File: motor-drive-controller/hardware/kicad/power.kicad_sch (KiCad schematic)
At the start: 3 parts

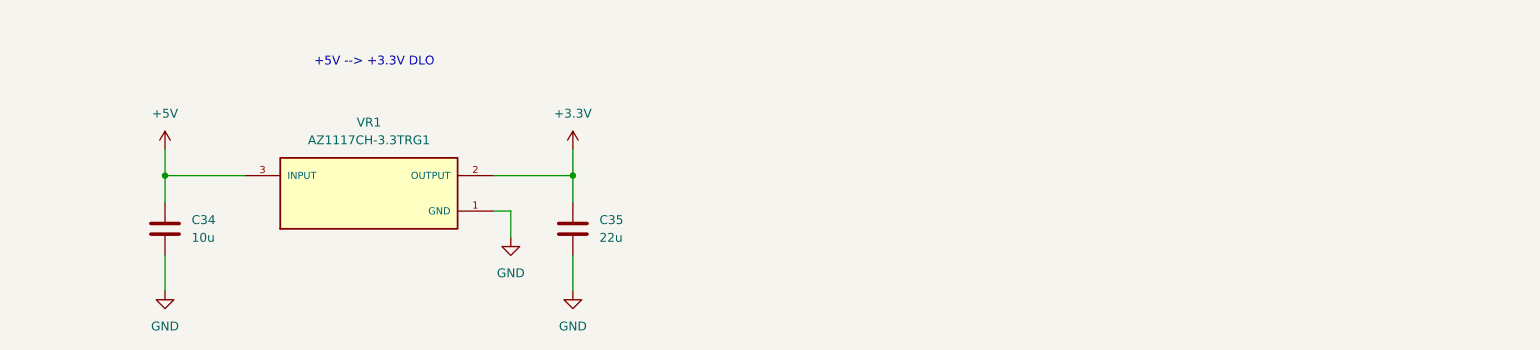
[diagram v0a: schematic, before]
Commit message: feat(hw10): add DC/DC-converter schema from 12V to 5V
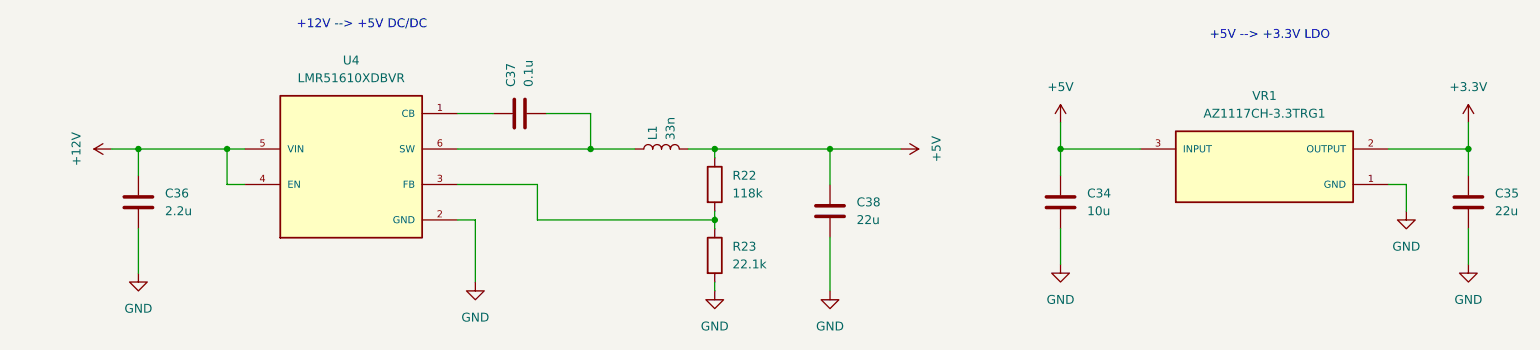
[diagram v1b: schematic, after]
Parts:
- added C36: 2.2u, Capacitor_SMD:C_0603_1608Metric, symbol Device:C
- added C37: 0.1u, Capacitor_SMD:C_0603_1608Metric, symbol Device:C
- added C38: 22u, Capacitor_SMD:C_0603_1608Metric, symbol Device:C
- added L1: 33n, symbol Device:L
- added R22: 118k, Resistor_SMD:R_0603_1608Metric, symbol Device:R
- added R23: 22.1k, Resistor_SMD:R_0603_1608Metric, symbol Device:R
- added U4: LMR51610XDBVR, LMR51610XDBVR:SOT95P280X145-6N, symbol LMR51610XDBVR:LMR51610XDBVR
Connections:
- net +5V: now also C38.1, L1.2, R22.1
- net GND: now also C36.2, C38.2, R23.2, U4.2 (GND)
- new net: C37.2, L1.1, U4.6 (SW)
- new net: C37.1, U4.1 (CB)
- new net: R22.2, R23.1, U4.3 (FB)
- new net +12V: C36.1, U4.4 (EN), U4.5 (VIN)
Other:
- note added: "+12V --> +5V DC/DC"
- note added: "+5V --> +3.3V LDO"
- note removed: "+5V --> +3.3V DLO"
- moved on the sheet: C34, C35, VR1

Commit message: fix(hw10): correct capacitor value from 33n to 33u in power schematic
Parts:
- L1: value 33n -> 33u
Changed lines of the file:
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@@
 			)
 		)
-		(property "Value" "33n"
+		(property "Value" "33u"
 			(at 114.2999 125.73 0)
 			(show_name no)

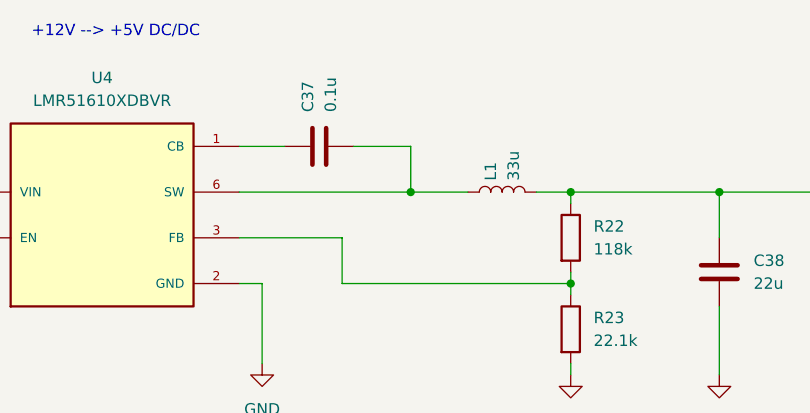
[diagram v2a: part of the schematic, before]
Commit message: fix(hw10): replace  inductor for XAL6060-333MEC
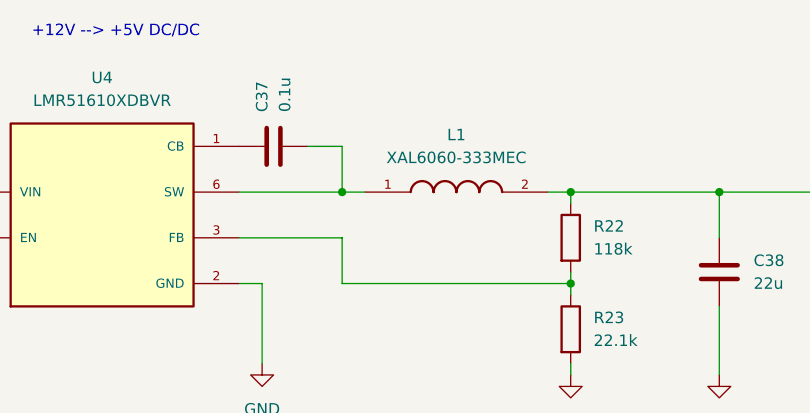
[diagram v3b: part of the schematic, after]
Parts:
- removed L1: 33u, symbol Device:L
- added L1: XAL6060-333MEC, XAL6060-333MEC:XAL6060333MEC, symbol XAL6060-333MEC:XAL6060-333MEC
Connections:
- net +5V: now also L1.2
- net at C37.2, U4.6 (SW): now also L1.1
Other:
- moved on the sheet: C37

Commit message: fix(hw10): update capacitor footprints and add voltage properties in power schematic
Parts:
- C34: footprint Capacitor_SMD:C_0603_1608Metric -> Capacitor_SMD:C_1206_3216Metric; Voltage (none) -> 16V
- C35: footprint Capacitor_SMD:C_0603_1608Metric -> Capacitor_SMD:C_0805_2012Metric; Voltage (none) -> 10V
- C36: footprint Capacitor_SMD:C_0603_1608Metric -> Capacitor_SMD:C_1206_3216Metric; Voltage (none) -> 50V
- C38: footprint Capacitor_SMD:C_0603_1608Metric -> Capacitor_SMD:C_1210_3225Metric; Voltage (none) -> 25V
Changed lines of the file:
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@@
 			)
 		)
-		(property "Footprint" "Capacitor_SMD:C_0603_1608Metric"
+		(property "Footprint" "Capacitor_SMD:C_1206_3216Metric"
 			(at 39.0652 138.43 0)
 			(hide yes)
@@
 			)
 		)
+		(property "Voltage" "50V"
+			(at 38.1 134.62 0)
+			(hide yes)
+			(show_name no)
+			(do_not_autoplace no)
+			(effects
+				(font
+					(size 1.27 1.27)
+				)
+			)
+		)
 		(pin "1"
 		)
@@
 			)
 		)
-		(property "Footprint" "Capacitor_SMD:C_0603_1608Metric"
+		(property "Footprint" "Capacitor_SMD:C_1210_3225Metric"
 			(at 138.1252 139.7 0)
 			(hide yes)
@@
 			)
 		)
+		(property "Voltage" "25V"
+			(at 137.16 135.89 0)
+			(hide yes)
+			(show_name no)
+			(do_not_autoplace no)
+			(effects
+				(font
+					(size 1.27 1.27)
+				)
+			)
+		)
 		(pin "1"
 		)
@@
 			)
 		)
-		(property "Footprint" "Capacitor_SMD:C_0603_1608Metric"
+		(property "Footprint" "Capacitor_SMD:C_0805_2012Metric"
 			(at 229.5652 138.43 0)
 			(hide yes)
@@
 			)
 		)
+		(property "Voltage" "10V"
+			(at 228.6 134.62 0)
+			(hide yes)
+			(show_name no)
+			(do_not_autoplace no)
+			(effects
+				(font
+					(size 1.27 1.27)
+				)
+			)
+		)
 		(pin "1"
 		)
@@
 			)
 		)
-		(property "Footprint" "Capacitor_SMD:C_0603_1608Metric"
+		(property "Footprint" "Capacitor_SMD:C_1206_3216Metric"
 			(at 171.1452 138.43 0)
 			(hide yes)
@@
 			(at 170.18 134.62 0)
 			(hide yes)
+			(show_name no)
+			(do_not_autoplace no)
+			(effects
+				(font
+					(size 1.27 1.27)
+				)
+			)
+		)
+		(property "Voltage" "16V"
+			(at 170.18 134.62 0)
+			(hide yes)

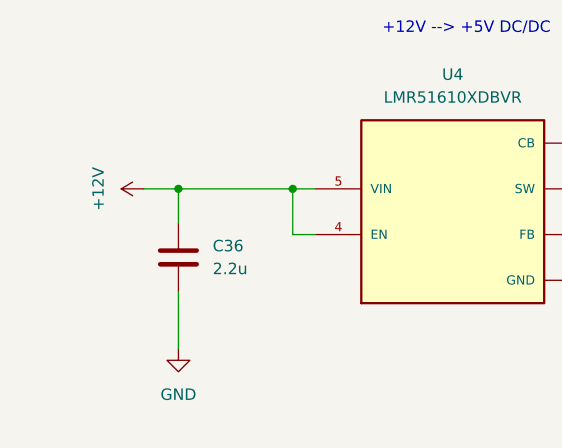
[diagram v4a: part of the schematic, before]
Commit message: fix(hw10): add 100nF capacitor for high-frequency filtering in power schematic
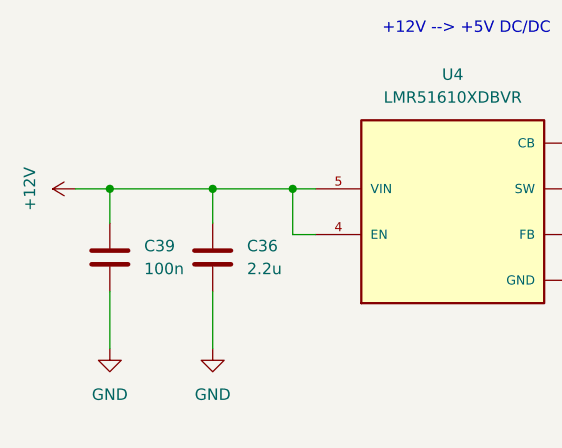
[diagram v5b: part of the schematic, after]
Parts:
- added C39: 100n, Capacitor_SMD:C_0603_1608Metric, symbol Device:C
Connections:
- net +12V: now also C39.1
- net GND: now also C39.2
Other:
- moved on the sheet: C36
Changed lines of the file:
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@@
+	)
+	(junction
+		(at 41.91 127)
+		(diameter 0)
+		(color 0 0 0 0)
 	)
 	(junction
@@
 	)
 	(junction
-		(at 38.1 127)
+		(at 30.48 127)
 		(diameter 0)
 		(color 0 0 0 0)
@@
 	(wire
 		(pts
+			(xy 30.48 138.43) (xy 30.48 144.78)
+		)
+		(stroke
+			(width 0)
+			(type default)
+		)
+	)
+	(wire
+		(pts
 			(xy 137.16 127) (xy 137.16 132.08)
 		)
@@
 	(wire
 		(pts
-			(xy 34.29 127) (xy 38.1 127)
+			(xy 26.67 127) (xy 30.48 127)
 		)
 		(stroke
@@
 	(wire
 		(pts
-			(xy 38.1 138.43) (xy 38.1 144.78)
+			(xy 41.91 138.43) (xy 41.91 144.78)
 		)
 		(stroke
@@
 	(wire
 		(pts
+			(xy 30.48 127) (xy 41.91 127)
+		)
+		(stroke
+			(width 0)
+			(type default)
+		)
+	)
+	(wire
+		(pts
 			(xy 118.11 127) (xy 120.65 127)
 		)
@@
 	(wire
 		(pts
-			(xy 38.1 127) (xy 38.1 130.81)
+			(xy 41.91 127) (xy 41.91 130.81)
 		)
 		(stroke
@@
 	(wire
 		(pts
+			(xy 30.48 127) (xy 30.48 130.81)
+		)
+		(stroke
+			(width 0)
+			(type default)
+		)
+	)
+	(wire
+		(pts
 			(xy 120.65 146.05) (xy 120.65 147.32)
 		)
@@
 	(wire
 		(pts
-			(xy 38.1 127) (xy 50.8 127)
-		)
-		(stroke
-			(width 0)
-			(type default)
-		)
-	)
-	(wire
-		(pts
 			(xy 91.44 121.92) (xy 95.25 121.92)
 		)
@@
 		(pts
 			(xy 120.65 135.89) (xy 120.65 137.16)
+		)
+		(stroke
+			(width 0)
+			(type default)
+		)
+	)
+	(wire
+		(pts
+			(xy 41.91 127) (xy 50.8 127)
 		)
 		(stroke
@@
 	(symbol
 		(lib_id "Device:C")
-		(at 38.1 134.62 0)
+		(at 41.91 134.62 0)
 		(unit 1)
 		(body_style 1)
@@
 		(fields_autoplaced yes)
 		(property "Reference" "C36"
-			(at 41.91 133.3499 0)
+			(at 45.72 133.3499 0)
 			(show_name no)
 			(do_not_autoplace no)
@@
 		)
 		(property "Value" "2.2u"
-			(at 41.91 135.8899 0)
+			(at 45.72 135.8899 0)
 			(show_name no)
 			(do_not_autoplace no)
@@
 		)
 		(property "Footprint" "Capacitor_SMD:C_1206_3216Metric"
-			(at 39.0652 138.43 0)
+			(at 42.8752 138.43 0)
 			(hide yes)
 			(show_name no)
@@
 		)
 		(property "Datasheet" ""
-			(at 38.1 134.62 0)
+			(at 41.91 134.62 0)
 			(hide yes)
 			(show_name no)
@@
 		)
 		(property "Description" "Unpolarized capacitor"
-			(at 38.1 134.62 0)
+			(at 41.91 134.62 0)
 			(hide yes)
 			(show_name no)
@@
 		)
 		(property "Voltage" "50V"
-			(at 38.1 134.62 0)
+			(at 41.91 134.62 0)
 			(hide yes)
 			(show_name no)
@@
 	)
 	(symbol
+		(lib_id "Device:C")
+		(at 30.48 134.62 0)
+		(unit 1)
+		(body_style 1)
+		(exclude_from_sim no)
+		(in_bom yes)
+		(on_board yes)
+		(in_pos_files yes)
+		(dnp no)
+		(fields_autoplaced yes)
+		(property "Reference" "C39"
+			(at 34.29 133.3499 0)
+			(show_name no)
+			(do_not_autoplace no)
+			(effects
+				(font
+					(size 1.27 1.27)
+				)
+				(justify left)
+			)
+		)
+		(property "Value" "100n"
+			(at 34.29 135.8899 0)
+			(show_name no)
+			(do_not_autoplace no)
+			(effects
+				(font
+					(size 1.27 1.27)
+				)
+				(justify left)
+			)
+		)
+		(property "Footprint" "Capacitor_SMD:C_0603_1608Metric"
+			(at 31.4452 138.43 0)
+			(hide yes)
+			(show_name no)
+			(do_not_autoplace no)
+			(effects
+				(font
+					(size 1.27 1.27)
+				)
+			)
+		)
+		(property "Datasheet" ""
+			(at 30.48 134.62 0)
+			(hide yes)
+			(show_name no)
+			(do_not_autoplace no)
+			(effects
+				(font
+					(size 1.27 1.27)
+				)
+			)
+		)
+		(property "Description" "Unpolarized capacitor"
+			(at 30.48 134.62 0)
+			(hide yes)
+			(show_name no)
+			(do_not_autoplace no)
+			(effects
+				(font
+					(size 1.27 1.27)
+				)
+			)
+		)
+		(pin "1"
+		)
+		(pin "2"
+		)
+		(instances
+			(project "motor-drive-controller"
+				(path "/b8e0307a-d356-4cd3-91c6-dd251b6e910b/4f45cab3-b4c2-456a-894e-61f49c3959a4"
+					(reference "C39")
+					(unit 1)
+				)
+			)
+		)
+	)
+	(symbol
 		(lib_id "power:GND")
 		(at 137.16 147.32 0)
@@
 	(symbol
 		(lib_id "power:GND")
-		(at 38.1 144.78 0)
+		(at 41.91 144.78 0)
 		(unit 1)
 		(body_style 1)
@@
 		(fields_autoplaced yes)
 		(property "Reference" "#PWR063"
-			(at 38.1 151.13 0)
+			(at 41.91 151.13 0)
 			(hide yes)
 			(show_name no)
@@
 		)
 		(property "Value" "GND"
-			(at 38.1 149.86 0)
+			(at 41.91 149.86 0)
 			(show_name no)
 			(do_not_autoplace no)
@@
 		)
 		(property "Footprint" ""
-			(at 38.1 144.78 0)
+			(at 41.91 144.78 0)
 			(hide yes)
 			(show_name no)
@@
 		)
 		(property "Datasheet" ""
-			(at 38.1 144.78 0)
+			(at 41.91 144.78 0)
 			(hide yes)
 			(show_name no)
@@
 		)
 		(property "Description" "Power symbol creates a global label with name \"GND\" , ground"
-			(at 38.1 144.78 0)
+			(at 41.91 144.78 0)
 			(hide yes)
 			(show_name no)
@@
 	(symbol
 		(lib_id "power:+12V")
-		(at 34.29 127 90)
+		(at 26.67 127 90)
 		(unit 1)
 		(body_style 1)
@@
 		(fields_autoplaced yes)
 		(property "Reference" "#PWR062"
-			(at 38.1 127 0)
+			(at 30.48 127 0)
 			(hide yes)
 			(show_name no)
@@
 		)
 		(property "Value" "+12V"
-			(at 29.21 127 0)
+			(at 21.59 127 0)
 			(show_name no)
 			(do_not_autoplace no)
@@
 		)
 		(property "Footprint" ""
-			(at 34.29 127 0)
+			(at 26.67 127 0)
 			(hide yes)
 			(show_name no)
@@
 		)
 		(property "Datasheet" ""
-			(at 34.29 127 0)
+			(at 26.67 127 0)
 			(hide yes)
 			(show_name no)
@@
 		)
 		(property "Description" "Power symbol creates a global label with name \"+12V\""
-			(at 34.29 127 0)
+			(at 26.67 127 0)
 			(hide yes)
 			(show_name no)
@@
 					(unit 1)
 				)
+			)
+		)
+	)
+	(symbol
+		(lib_id "power:GND")
+		(at 30.48 144.78 0)
+		(unit 1)
+		(body_style 1)
+		(exclude_from_sim no)
+		(in_bom yes)
+		(on_board yes)
+		(in_pos_files yes)
+		(dnp no)
+		(fields_autoplaced yes)
+		(property "Reference" "#PWR068"
+			(at 30.48 151.13 0)
+			(hide yes)
+			(show_name no)
+			(do_not_autoplace no)
+			(effects
+				(font
+					(size 1.27 1.27)
+				)
+			)
+		)
+		(property "Value" "GND"
+			(at 30.48 149.86 0)
+			(show_name no)
+			(do_not_autoplace no)
+			(effects
+				(font
+					(size 1.27 1.27)
+				)
+			)
+		)
+		(property "Footprint" ""
+			(at 30.48 144.78 0)
+			(hide yes)
+			(show_name no)
+			(do_not_autoplace no)
+			(effects
+				(font
+					(size 1.27 1.27)
+				)
+			)
+		)
+		(property "Datasheet" ""
+			(at 30.48 144.78 0)
+			(hide yes)
+			(show_name no)
+			(do_not_autoplace no)
+			(effects
+				(font
+					(size 1.27 1.27)
+				)
+			)
+		)
+		(property "Description" "Power symbol creates a global label with name \"GND\" , ground"
+			(at 30.48 144.78 0)
+			(hide yes)
+			(show_name no)
+			(do_not_autoplace no)
+			(effects
+				(font
+					(size 1.27 1.27)
+				)
+			)
+		)
+		(pin "1"
+		)
+		(instances
+			(project "motor-drive-controller"
+				(path "/b8e0307a-d356-4cd3-91c6-dd251b6e910b/4f45cab3-b4c2-456a-894e-61f49c3959a4"
+					(reference "#PWR068")
+					(unit 1)
+				)

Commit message: fix(hw10): reset existing annotation
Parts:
- renumbered C39 to C34, C36 to C35, C37 to C36, C38 to C37, C34 to C38, C35 to C39
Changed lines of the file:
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@@
 		(dnp no)
 		(fields_autoplaced yes)
-		(property "Reference" "C36"
+		(property "Reference" "C35"
 			(at 45.72 133.3499 0)
 			(show_name no)
@@
 			(project "motor-drive-controller"
 				(path "/b8e0307a-d356-4cd3-91c6-dd251b6e910b/4f45cab3-b4c2-456a-894e-61f49c3959a4"
-					(reference "C36")
+					(reference "C35")
 					(unit 1)
 				)
@@
 		(dnp no)
 		(fields_autoplaced yes)
-		(property "Reference" "C38"
+		(property "Reference" "C37"
 			(at 140.97 134.6199 0)
 			(show_name no)
@@
 			(project "motor-drive-controller"
 				(path "/b8e0307a-d356-4cd3-91c6-dd251b6e910b/4f45cab3-b4c2-456a-894e-61f49c3959a4"
-					(reference "C38")
+					(reference "C37")
 					(unit 1)
 				)
@@
 		(dnp no)
 		(fields_autoplaced yes)
-		(property "Reference" "C35"
+		(property "Reference" "C39"
 			(at 232.41 133.3499 0)
 			(show_name no)
@@
 			(project "motor-drive-controller"
 				(path "/b8e0307a-d356-4cd3-91c6-dd251b6e910b/4f45cab3-b4c2-456a-894e-61f49c3959a4"
-					(reference "C35")
+					(reference "C39")
 					(unit 1)
 				)
@@
 		(dnp no)
 		(fields_autoplaced yes)
-		(property "Reference" "#PWR066"
+		(property "Reference" "#PWR061"
 			(at 120.65 153.67 0)
 			(hide yes)
@@
 			(project "motor-drive-controller"
 				(path "/b8e0307a-d356-4cd3-91c6-dd251b6e910b/4f45cab3-b4c2-456a-894e-61f49c3959a4"
-					(reference "#PWR066")
+					(reference "#PWR061")
 					(unit 1)
 				)
@@
 		(dnp no)
 		(fields_autoplaced yes)
-		(property "Reference" "#PWR060"
+		(property "Reference" "#PWR065"
 			(at 170.18 149.86 0)
 			(hide yes)
@@
 			(project "motor-drive-controller"
 				(path "/b8e0307a-d356-4cd3-91c6-dd251b6e910b/4f45cab3-b4c2-456a-894e-61f49c3959a4"
-					(reference "#PWR060")
+					(reference "#PWR065")
 					(unit 1)
 				)
@@
 		(dnp no)
 		(fields_autoplaced yes)
-		(property "Reference" "#PWR059"
+		(property "Reference" "#PWR066"
 			(at 219.71 142.24 0)
 			(hide yes)
@@
 			(project "motor-drive-controller"
 				(path "/b8e0307a-d356-4cd3-91c6-dd251b6e910b/4f45cab3-b4c2-456a-894e-61f49c3959a4"
-					(reference "#PWR059")
+					(reference "#PWR066")
 					(unit 1)
 				)
@@
 		(dnp no)
 		(fields_autoplaced yes)
-		(property "Reference" "C39"
+		(property "Reference" "C34"
 			(at 34.29 133.3499 0)
 			(show_name no)
@@
 			(project "motor-drive-controller"
 				(path "/b8e0307a-d356-4cd3-91c6-dd251b6e910b/4f45cab3-b4c2-456a-894e-61f49c3959a4"
-					(reference "C39")
+					(reference "C34")
 					(unit 1)
 				)
@@
 		(dnp no)
 		(fields_autoplaced yes)
-		(property "Reference" "#PWR067"
+		(property "Reference" "#PWR062"
 			(at 137.16 153.67 0)
 			(hide yes)
@@
 			(project "motor-drive-controller"
 				(path "/b8e0307a-d356-4cd3-91c6-dd251b6e910b/4f45cab3-b4c2-456a-894e-61f49c3959a4"
-					(reference "#PWR067")
+					(reference "#PWR062")
 					(unit 1)
 				)
@@
 		(dnp no)
 		(fields_autoplaced yes)
-		(property "Reference" "#PWR061"
+		(property "Reference" "#PWR068"
 			(at 228.6 149.86 0)
 			(hide yes)
@@
 			(project "motor-drive-controller"
 				(path "/b8e0307a-d356-4cd3-91c6-dd251b6e910b/4f45cab3-b4c2-456a-894e-61f49c3959a4"
-					(reference "#PWR061")
+					(reference "#PWR068")
 					(unit 1)
 				)
@@
 		(dnp no)
 		(fields_autoplaced yes)
-		(property "Reference" "C34"
+		(property "Reference" "C38"
 			(at 173.99 133.3499 0)
 			(show_name no)
@@
 			(project "motor-drive-controller"
 				(path "/b8e0307a-d356-4cd3-91c6-dd251b6e910b/4f45cab3-b4c2-456a-894e-61f49c3959a4"
-					(reference "C34")
+					(reference "C38")
 					(unit 1)
 				)
@@
 		(dnp no)
 		(fields_autoplaced yes)
-		(property "Reference" "#PWR058"
+		(property "Reference" "#PWR067"
 			(at 228.6 127 0)
 			(hide yes)
@@
 			(project "motor-drive-controller"
 				(path "/b8e0307a-d356-4cd3-91c6-dd251b6e910b/4f45cab3-b4c2-456a-894e-61f49c3959a4"
-					(reference "#PWR058")
+					(reference "#PWR067")
 					(unit 1)
 				)
@@
 		(dnp no)
 		(fields_autoplaced yes)
-		(property "Reference" "#PWR063"
+		(property "Reference" "#PWR059"
 			(at 41.91 151.13 0)
 			(hide yes)
@@
 			(project "motor-drive-controller"
 				(path "/b8e0307a-d356-4cd3-91c6-dd251b6e910b/4f45cab3-b4c2-456a-894e-61f49c3959a4"
-					(reference "#PWR063")
+					(reference "#PWR059")
 					(unit 1)
 				)
@@
 		(dnp no)
 		(fields_autoplaced yes)
-		(property "Reference" "#PWR062"
+		(property "Reference" "#PWR057"
 			(at 30.48 127 0)
 			(hide yes)
@@
 			(project "motor-drive-controller"
 				(path "/b8e0307a-d356-4cd3-91c6-dd251b6e910b/4f45cab3-b4c2-456a-894e-61f49c3959a4"
-					(reference "#PWR062")
+					(reference "#PWR057")
 					(unit 1)
 				)
@@
 		(dnp no)
 		(fields_autoplaced yes)
-		(property "Reference" "C37"
+		(property "Reference" "C36"
 			(at 86.3599 118.11 0)
 			(show_name no)
@@
 			(project "motor-drive-controller"
 				(path "/b8e0307a-d356-4cd3-91c6-dd251b6e910b/4f45cab3-b4c2-456a-894e-61f49c3959a4"
-					(reference "C37")
+					(reference "C36")
 					(unit 1)
 				)
@@
 		(dnp no)
 		(fields_autoplaced yes)
-		(property "Reference" "#PWR065"
+		(property "Reference" "#PWR063"
 			(at 143.51 127 0)
 			(hide yes)
@@
 			(project "motor-drive-controller"
 				(path "/b8e0307a-d356-4cd3-91c6-dd251b6e910b/4f45cab3-b4c2-456a-894e-61f49c3959a4"
-					(reference "#PWR065")
+					(reference "#PWR063")
 					(unit 1)
 				)
@@
 		(dnp no)
 		(fields_autoplaced yes)
-		(property "Reference" "#PWR068"
+		(property "Reference" "#PWR058"
 			(at 30.48 151.13 0)
 			(hide yes)
@@
 			(project "motor-drive-controller"
 				(path "/b8e0307a-d356-4cd3-91c6-dd251b6e910b/4f45cab3-b4c2-456a-894e-61f49c3959a4"
-					(reference "#PWR068")
+					(reference "#PWR058")
 					(unit 1)
 				)
@@
 		(dnp no)
 		(fields_autoplaced yes)
-		(property "Reference" "#PWR057"
+		(property "Reference" "#PWR064"
 			(at 170.18 127 0)
 			(hide yes)
@@
 			(project "motor-drive-controller"
 				(path "/b8e0307a-d356-4cd3-91c6-dd251b6e910b/4f45cab3-b4c2-456a-894e-61f49c3959a4"
-					(reference "#PWR057")
+					(reference "#PWR064")
 					(unit 1)
 				)
@@
 		(dnp no)
 		(fields_autoplaced yes)
-		(property "Reference" "#PWR064"
+		(property "Reference" "#PWR060"
 			(at 86.36 152.4 0)
 			(hide yes)
@@
 			(project "motor-drive-controller"
 				(path "/b8e0307a-d356-4cd3-91c6-dd251b6e910b/4f45cab3-b4c2-456a-894e-61f49c3959a4"
-					(reference "#PWR064")
-					(unit 1)
-				)
+					(reference "#PWR060")
+					(unit 1)
+				)
